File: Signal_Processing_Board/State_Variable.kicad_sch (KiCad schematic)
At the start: 31 parts, among them U10 TL082, U4 TL084

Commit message: Final version of the board, updated with lessons from first version
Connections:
- net +15V: now also C19.2, U4.4 (V+); no longer C20.2, U4.11 (V-)
- net -15V: now also C20.2, U4.11 (V-); no longer C19.2, U4.4 (V+)
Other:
- moved on the sheet: C19, C20, U4E
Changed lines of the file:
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@@
 	)
 	(junction
-		(at 30.48 176.53)
-		(diameter 0)
-		(color 0 0 0 0)
-	)
-	(junction
 		(at 171.45 39.37)
 		(diameter 0)
@@
 	)
 	(junction
-		(at 30.48 158.75)
-		(diameter 0)
-		(color 0 0 0 0)
-	)
-	(junction
 		(at 120.65 113.03)
 		(diameter 0)
@@
 	)
 	(junction
+		(at 30.48 158.75)
+		(diameter 0)
+		(color 0 0 0 0)
+	)
+	(junction
 		(at 147.32 50.8)
 		(diameter 0)
@@
 	)
 	(junction
+		(at 30.48 176.53)
+		(diameter 0)
+		(color 0 0 0 0)
+	)
+	(junction
 		(at 185.42 146.05)
 		(diameter 0)
@@
 	(wire
 		(pts
-			(xy 30.48 176.53) (xy 30.48 175.26)
-		)
-		(stroke
-			(width 0)
-			(type default)
-		)
-	)
-	(wire
-		(pts
 			(xy 99.06 57.15) (xy 99.06 48.26)
 		)
@@
 	(wire
 		(pts
-			(xy 40.64 177.8) (xy 40.64 176.53)
-		)
-		(stroke
-			(width 0)
-			(type default)
-		)
-	)
-	(wire
-		(pts
 			(xy 147.32 39.37) (xy 147.32 50.8)
 		)
@@
 	(wire
 		(pts
-			(xy 143.51 115.57) (xy 148.59 115.57)
+			(xy 40.64 158.75) (xy 40.64 160.02)
 		)
 		(stroke
@@
 	(wire
 		(pts
-			(xy 182.88 53.34) (xy 187.96 53.34)
+			(xy 143.51 115.57) (xy 148.59 115.57)
 		)
 		(stroke
@@
 	(wire
 		(pts
-			(xy 40.64 160.02) (xy 40.64 158.75)
+			(xy 182.88 53.34) (xy 187.96 53.34)
 		)
 		(stroke
@@
 	(wire
 		(pts
-			(xy 30.48 158.75) (xy 30.48 160.02)
-		)
-		(stroke
-			(width 0)
-			(type default)
-		)
-	)
-	(wire
-		(pts
 			(xy 134.62 72.39) (xy 143.51 72.39)
 		)
@@
 	(wire
 		(pts
+			(xy 40.64 176.53) (xy 40.64 177.8)
+		)
+		(stroke
+			(width 0)
+			(type default)
+		)
+	)
+	(wire
+		(pts
 			(xy 110.49 54.61) (xy 110.49 53.34)
 		)
@@
 	(wire
 		(pts
+			(xy 30.48 158.75) (xy 30.48 160.02)
+		)
+		(stroke
+			(width 0)
+			(type default)
+		)
+	)
+	(wire
+		(pts
 			(xy 143.51 115.57) (xy 138.43 115.57)
 		)
@@
 	(wire
 		(pts
+			(xy 30.48 175.26) (xy 30.48 176.53)
+		)
+		(stroke
+			(width 0)
+			(type default)
+		)
+	)
+	(wire
+		(pts
 			(xy 165.1 148.59) (xy 166.37 148.59)
 		)
@@
 	(symbol
 		(lib_id "Device:C")
-		(at 40.64 163.83 180)
+		(at 40.64 181.61 180)
 		(unit 1)
 		(exclude_from_sim no)
@@
 		(fields_autoplaced yes)
 		(property "Reference" "C20"
-			(at 44.45 162.5599 0)
+			(at 44.45 180.3399 0)
 			(effects
 				(font
@@
 		)
 		(property "Value" "Cdec10"
-			(at 44.45 165.0999 0)
+			(at 44.45 182.8799 0)
 			(effects
 				(font
@@
 		)
 		(property "Footprint" "Capacitor_THT:C_Disc_D3.0mm_W1.6mm_P2.50mm"
-			(at 39.6748 160.02 0)
+			(at 39.6748 177.8 0)
 			(effects
 				(font
@@
 		)
 		(property "Datasheet" "~"
-			(at 40.64 163.83 0)
+			(at 40.64 181.61 0)
 			(effects
 				(font
@@
 		)
 		(property "Description" "Unpolarized capacitor"
-			(at 40.64 163.83 0)
+			(at 40.64 181.61 0)
 			(effects
 				(font
@@
 	(symbol
 		(lib_id "power:GND")
-		(at 40.64 185.42 0)
+		(at 40.64 167.64 0)
 		(unit 1)
 		(exclude_from_sim no)
@@
 		(fields_autoplaced yes)
 		(property "Reference" "#PWR033"
-			(at 40.64 191.77 0)
+			(at 40.64 173.99 0)
 			(effects
 				(font
@@
 		)
 		(property "Value" "GND"
-			(at 40.64 190.5 0)
+			(at 40.64 172.72 0)
 			(effects
 				(font
@@
 		)
 		(property "Footprint" ""
-			(at 40.64 185.42 0)
+			(at 40.64 167.64 0)
 			(effects
 				(font
@@
 		)
 		(property "Datasheet" ""
-			(at 40.64 185.42 0)
+			(at 40.64 167.64 0)
 			(effects
 				(font
@@
 		)
 		(property "Description" "Power symbol creates a global label with name \"GND\" , ground"
-			(at 40.64 185.42 0)
+			(at 40.64 167.64 0)
 			(effects
 				(font
@@
 	(symbol
 		(lib_id "power:GND")
-		(at 40.64 167.64 0)
+		(at 40.64 185.42 0)
 		(unit 1)
 		(exclude_from_sim no)
@@
 		(fields_autoplaced yes)
 		(property "Reference" "#PWR034"
-			(at 40.64 173.99 0)
+			(at 40.64 191.77 0)
 			(effects
 				(font
@@
 		)
 		(property "Value" "GND"
-			(at 40.64 172.72 0)
+			(at 40.64 190.5 0)
 			(effects
 				(font
@@
 		)
 		(property "Footprint" ""
-			(at 40.64 167.64 0)
+			(at 40.64 185.42 0)
 			(effects
 				(font
@@
 		)
 		(property "Datasheet" ""
-			(at 40.64 167.64 0)
+			(at 40.64 185.42 0)
 			(effects
 				(font
@@
 		)
 		(property "Description" "Power symbol creates a global label with name \"GND\" , ground"
-			(at 40.64 167.64 0)
+			(at 40.64 185.42 0)
 			(effects
 				(font
@@
 	(symbol
 		(lib_id "Device:C")
-		(at 40.64 181.61 180)
+		(at 40.64 163.83 180)
 		(unit 1)
 		(exclude_from_sim no)
@@
 		(fields_autoplaced yes)
 		(property "Reference" "C19"
-			(at 44.45 180.3399 0)
+			(at 44.45 162.5599 0)
 			(effects
 				(font
@@
 		)
 		(property "Value" "Cdec9"
-			(at 44.45 182.8799 0)
+			(at 44.45 165.0999 0)
 			(effects
 				(font
@@
 		)
 		(property "Footprint" "Capacitor_THT:C_Disc_D3.0mm_W1.6mm_P2.50mm"
-			(at 39.6748 177.8 0)
+			(at 39.6748 160.02 0)
 			(effects
 				(font
@@
 		)
 		(property "Datasheet" "~"
-			(at 40.64 181.61 0)
+			(at 40.64 163.83 0)
 			(effects
 				(font
@@
 		)
 		(property "Description" "Unpolarized capacitor"
-			(at 40.64 181.61 0)
+			(at 40.64 163.83 0)
 			(effects
 				(font
@@
 	(symbol
 		(lib_id "Amplifier_Operational:TL084")
-		(at 27.94 167.64 180)
+		(at 33.02 167.64 0)
 		(unit 5)
 		(exclude_from_sim no)
@@
 					(size 1.27 1.27)
 				)
-				(justify right)
+				(justify left)
 			)
 		)
@@
 					(size 1.27 1.27)
 				)
-				(justify right)
+				(justify left)
 			)
 		)
 		(property "Footprint" "Package_DIP:CERDIP-14_W7.62mm_SideBrazed_LongPads_Socket"
-			(at 29.21 170.18 0)
+			(at 31.75 165.1 0)
 			(effects
 				(font
@@
 		)
 		(property "Datasheet" "http://www.ti.com/lit/ds/symlink/tl081.pdf"
-			(at 26.67 172.72 0)
+			(at 34.29 162.56 0)
 			(effects
 				(font
@@
 		)
 		(property "Description" "Quad JFET-Input Operational Amplifiers, DIP-14/SOIC-14/SSOP-14"
-			(at 27.94 167.64 0)
+			(at 33.02 167.64 0)
 			(effects
 				(font

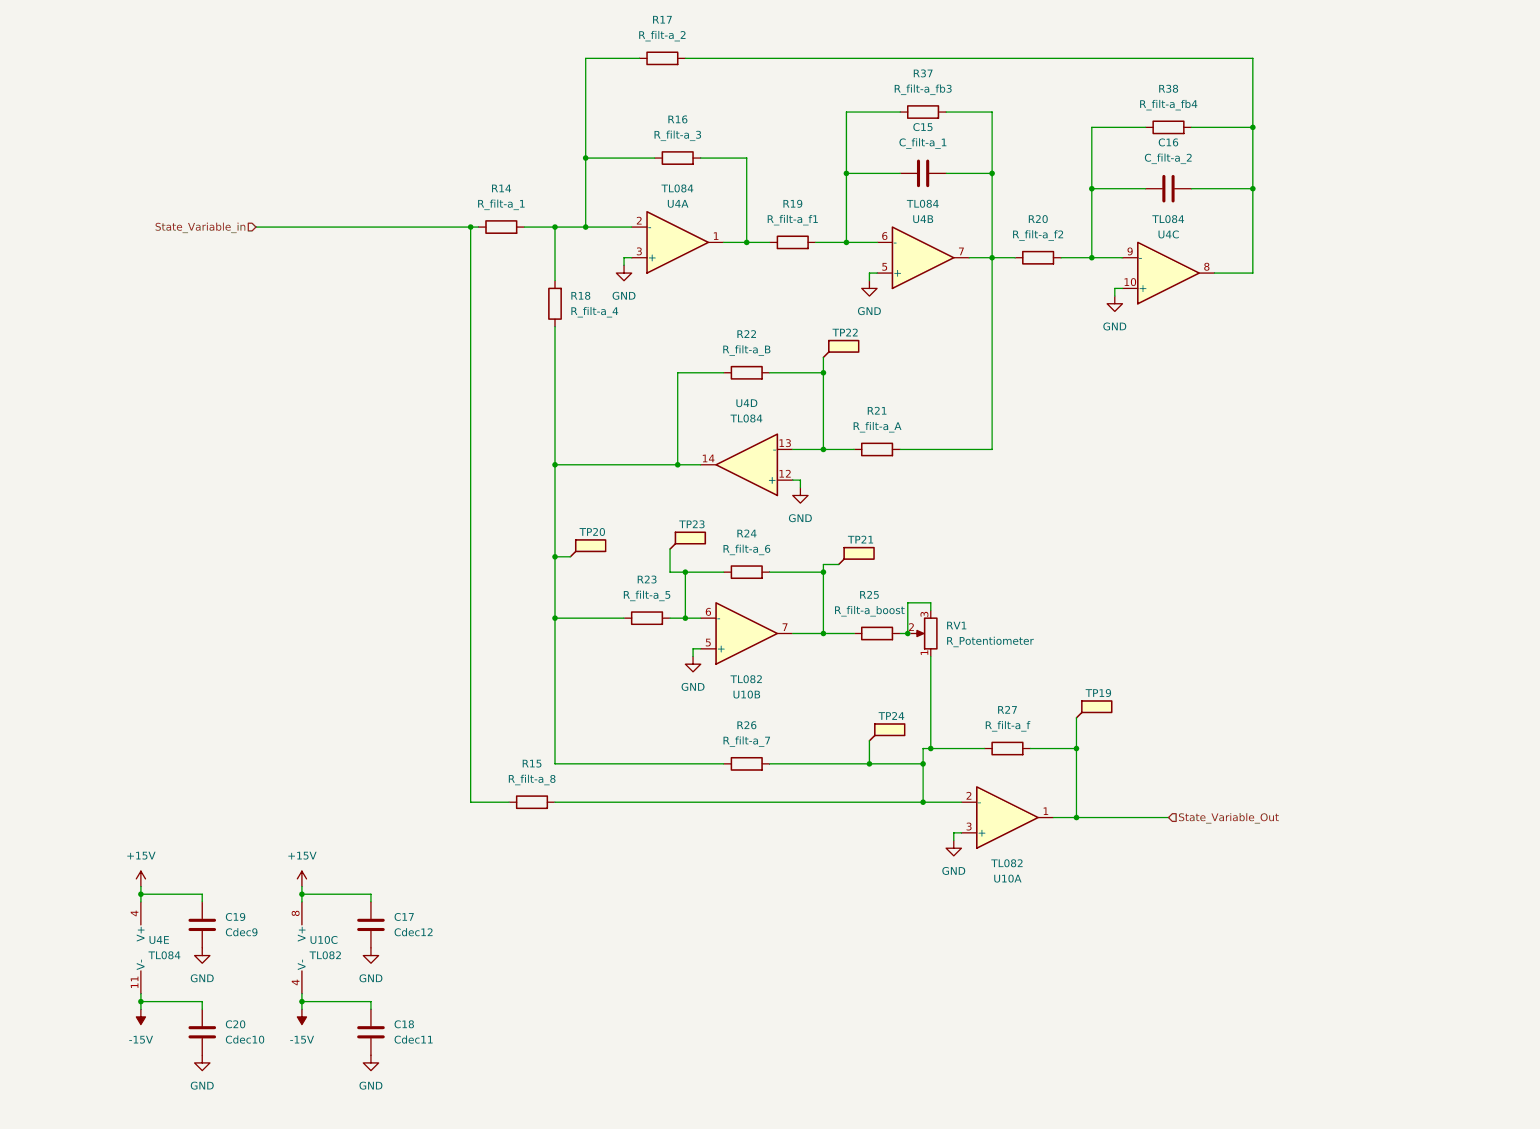
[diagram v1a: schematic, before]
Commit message: Updated file structure and added PDF of schematic
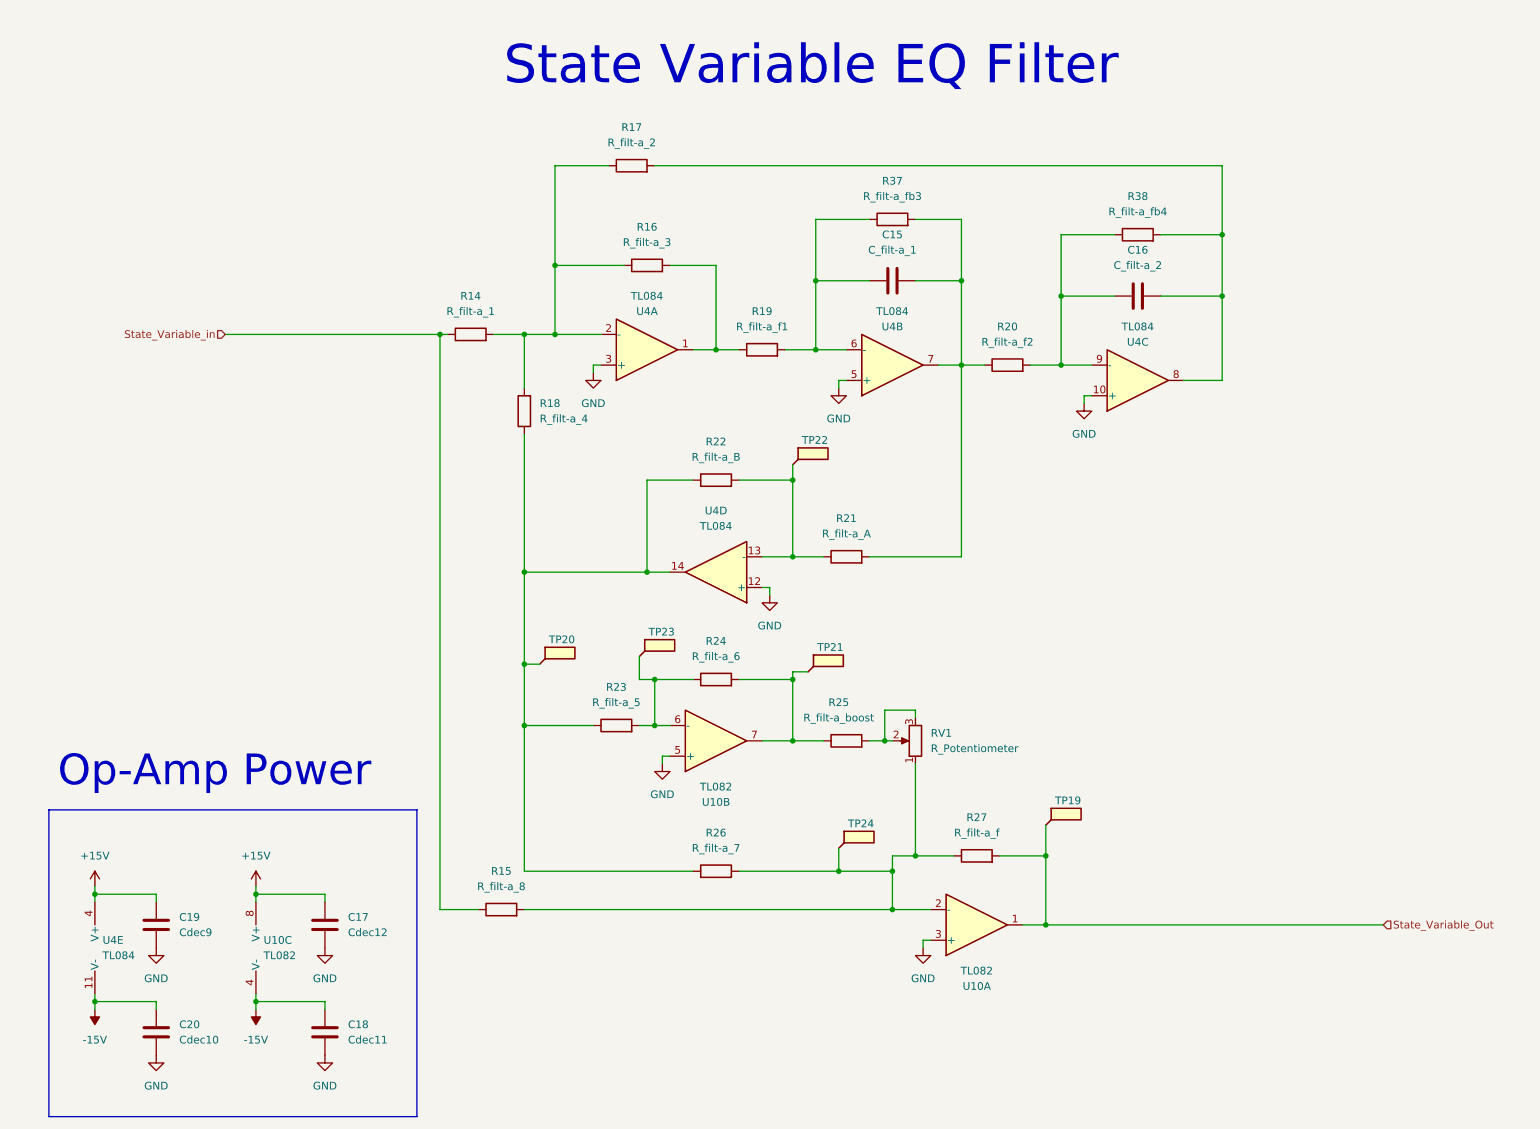
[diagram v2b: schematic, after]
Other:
- note added: "Op-Amp Power"
- note added: "State Variable EQ Filter"
- moved on the sheet: C15, C16, C17, C18, C19, C20, R14, R15, R16, R17, R18, R19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
